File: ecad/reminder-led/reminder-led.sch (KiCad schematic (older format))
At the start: 11 parts, among them J3 MOLEX SL 1x5, Q2 2N3904, Q3 2N3904, Q4 2N3904

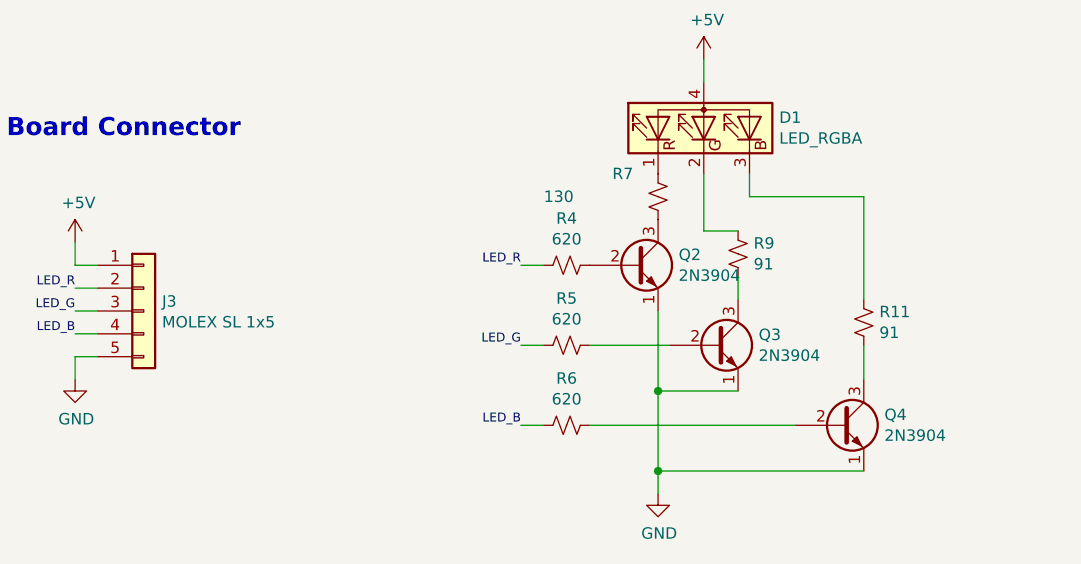
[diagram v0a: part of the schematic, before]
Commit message: Broke out file structure for separate boards
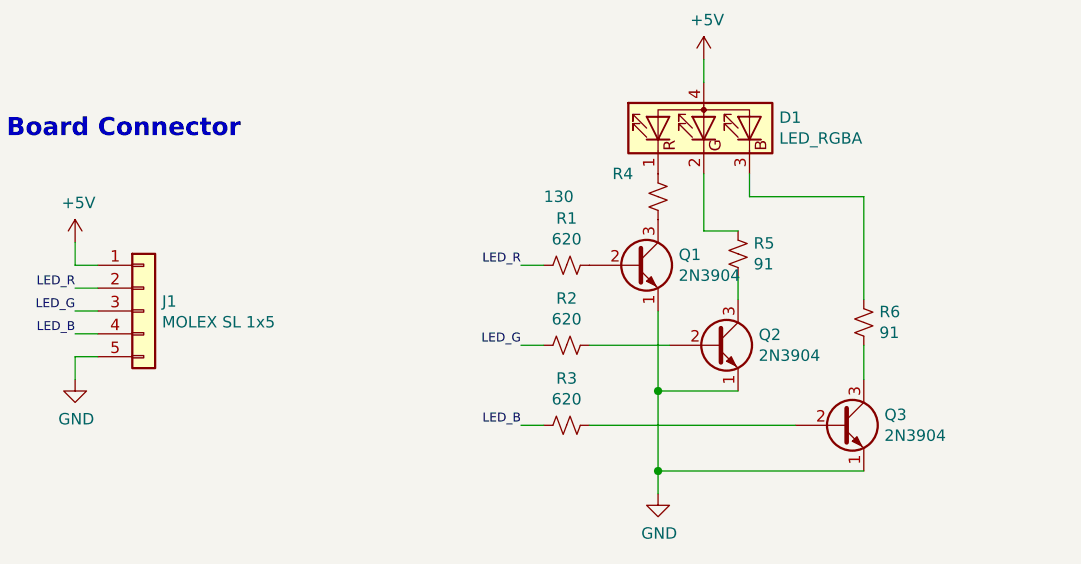
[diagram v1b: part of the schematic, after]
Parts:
- J1: renamed from J3; DNP (none) -> 1
- Q1: renamed from Q2; DNP (none) -> 1
- Q2: renamed from Q3; DNP (none) -> 1
- Q3: renamed from Q4; DNP (none) -> 1
- R1: renamed from R4; footprint Resistor_THT:R_Axial_DIN0204_L3.6mm_D1.6mm_P5.08mm_Horizontal -> R_Axial_DIN0204_L3.6mm_D1.6mm_P5.08mm_Horizontal; DNP (none) -> 1
- R2: renamed from R5; footprint Resistor_THT:R_Axial_DIN0204_L3.6mm_D1.6mm_P5.08mm_Horizontal -> R_Axial_DIN0204_L3.6mm_D1.6mm_P5.08mm_Horizontal; DNP (none) -> 1
- R3: renamed from R6; footprint Resistor_THT:R_Axial_DIN0204_L3.6mm_D1.6mm_P5.08mm_Horizontal -> R_Axial_DIN0204_L3.6mm_D1.6mm_P5.08mm_Horizontal; DNP (none) -> 1
- R4: renamed from R7; DNP (none) -> 1
- R5: renamed from R9; DNP (none) -> 1
- R6: renamed from R11; DNP (none) -> 1
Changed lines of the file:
@@
 P 6400 2650
 AR Path="/607C1B9E" Ref="#PWR?"  Part="1"
-AR Path="/60793C3B/607C1B9E" Ref="#PWR0107"  Part="1"
-F 0 "#PWR0107" H 6400 2500 50  0001 C CNN
+AR Path="/60793C3B/607C1B9E" Ref="#PWR04"  Part="1"
+F 0 "#PWR04" H 6400 2500 50  0001 C CNN
 F 1 "+5V" H 6415 2823 50  0000 C CNN
 F 2 "" H 6400 2650 50  0001 C CNN
@@
 P 5800 4250
 AR Path="/607C1BA9" Ref="R?"  Part="1"
-AR Path="/60793C3B/607C1BA9" Ref="R6"  Part="1"
-F 0 "R6" V 6005 4250 50  0000 C CNN
+AR Path="/60793C3B/607C1BA9" Ref="R3"  Part="1"
+F 0 "R3" V 6005 4250 50  0000 C CNN
 F 1 "620" V 5914 4250 50  0000 C CNN
-F 2 "Resistor_THT:R_Axial_DIN0204_L3.6mm_D1.6mm_P5.08mm_Horizontal" H 5800 4250 50  0001 C CNN
+F 2 "R_Axial_DIN0204_L3.6mm_D1.6mm_P5.08mm_Horizontal" H 5800 4250 50  0001 C CNN
 F 3 "~" H 5800 4250 50  0001 C CNN
 F 4 "Vishay" H 5800 4250 50  0001 C CNN "Mfg"
 F 5 "MBA02040C6200FC100" H 5800 4250 50  0001 C CNN "Mfg PN"
+F 6 "1" H 5800 4250 50  0001 C CNN "DNP"
 	1    5800 4250
 	0    -1   -1   0
@@
 P 5800 3900
 AR Path="/607C1BB1" Ref="R?"  Part="1"
-AR Path="/60793C3B/607C1BB1" Ref="R5"  Part="1"
-F 0 "R5" V 6005 3900 50  0000 C CNN
+AR Path="/60793C3B/607C1BB1" Ref="R2"  Part="1"
+F 0 "R2" V 6005 3900 50  0000 C CNN
 F 1 "620" V 5914 3900 50  0000 C CNN
-F 2 "Resistor_THT:R_Axial_DIN0204_L3.6mm_D1.6mm_P5.08mm_Horizontal" H 5800 3900 50  0001 C CNN
+F 2 "R_Axial_DIN0204_L3.6mm_D1.6mm_P5.08mm_Horizontal" H 5800 3900 50  0001 C CNN
 F 3 "~" H 5800 3900 50  0001 C CNN
 F 4 "Vishay" H 5800 3900 50  0001 C CNN "Mfg"
 F 5 "MBA02040C6200FC100" H 5800 3900 50  0001 C CNN "Mfg PN"
+F 6 "1" H 5800 3900 50  0001 C CNN "DNP"
 	1    5800 3900
 	0    -1   -1   0
@@
 P 5800 3550
 AR Path="/607C1BB9" Ref="R?"  Part="1"
-AR Path="/60793C3B/607C1BB9" Ref="R4"  Part="1"
-F 0 "R4" V 6005 3550 50  0000 C CNN
+AR Path="/60793C3B/607C1BB9" Ref="R1"  Part="1"
+F 0 "R1" V 6005 3550 50  0000 C CNN
 F 1 "620" V 5914 3550 50  0000 C CNN
-F 2 "Resistor_THT:R_Axial_DIN0204_L3.6mm_D1.6mm_P5.08mm_Horizontal" H 5800 3550 50  0001 C CNN
+F 2 "R_Axial_DIN0204_L3.6mm_D1.6mm_P5.08mm_Horizontal" H 5800 3550 50  0001 C CNN
 F 3 "~" H 5800 3550 50  0001 C CNN
 F 4 "Vishay" H 5800 3550 50  0001 C CNN "Mfg"
 F 5 "MBA02040C6200FC100" H 5800 3550 50  0001 C CNN "Mfg PN"
+F 6 "1" H 5800 3550 50  0001 C CNN "DNP"
 	1    5800 3550
 	0    -1   -1   0
@@
 P 6200 4550
 AR Path="/607C1BC6" Ref="#PWR?"  Part="1"
-AR Path="/60793C3B/607C1BC6" Ref="#PWR0110"  Part="1"
-F 0 "#PWR0110" H 6200 4300 50  0001 C CNN
+AR Path="/60793C3B/607C1BC6" Ref="#PWR03"  Part="1"
+F 0 "#PWR03" H 6200 4300 50  0001 C CNN
 F 1 "GND" H 6205 4377 50  0000 C CNN
 F 2 "" H 6200 4550 50  0001 C CNN
@@
 P 7100 3800
 AR Path="/607C1BD3" Ref="R?"  Part="1"
-AR Path="/60793C3B/607C1BD3" Ref="R11"  Part="1"
-F 0 "R11" H 7168 3846 50  0000 L CNN
+AR Path="/60793C3B/607C1BD3" Ref="R6"  Part="1"
+F 0 "R6" H 7168 3846 50  0000 L CNN
 F 1 "91" H 7168 3755 50  0000 L CNN
 F 2 "Resistor_THT:R_Axial_DIN0204_L3.6mm_D1.6mm_P5.08mm_Horizontal" H 7100 3800 50  0001 C CNN
 F 3 "~" H 7100 3800 50  0001 C CNN
+F 4 "1" H 7100 3800 50  0001 C CNN "DNP"
 	1    7100 3800
 	1    0    0    -1
@@
 P 6550 3500
 AR Path="/607C1BD9" Ref="R?"  Part="1"
-AR Path="/60793C3B/607C1BD9" Ref="R9"  Part="1"
-F 0 "R9" H 6618 3546 50  0000 L CNN
+AR Path="/60793C3B/607C1BD9" Ref="R5"  Part="1"
+F 0 "R5" H 6618 3546 50  0000 L CNN
 F 1 "91" H 6618 3455 50  0000 L CNN
 F 2 "Resistor_THT:R_Axial_DIN0204_L3.6mm_D1.6mm_P5.08mm_Horizontal" H 6550 3500 50  0001 C CNN
 F 3 "~" H 6550 3500 50  0001 C CNN
+F 4 "1" H 6550 3500 50  0001 C CNN "DNP"
 	1    6550 3500
 	1    0    0    -1
@@
 P 6200 3250
 AR Path="/607C1BDF" Ref="R?"  Part="1"
-AR Path="/60793C3B/607C1BDF" Ref="R7"  Part="1"
-F 0 "R7" H 6000 3350 50  0000 L CNN
+AR Path="/60793C3B/607C1BDF" Ref="R4"  Part="1"
+F 0 "R4" H 6000 3350 50  0000 L CNN
 F 1 "130" H 5700 3250 50  0000 L CNN
 F 2 "Resistor_THT:R_Axial_DIN0204_L3.6mm_D1.6mm_P5.08mm_Horizontal" H 6200 3250 50  0001 C CNN
 F 3 "~" H 6200 3250 50  0001 C CNN
+F 4 "1" H 6200 3250 50  0001 C CNN "DNP"
 	1    6200 3250
 	1    0    0    -1
@@
 P 7000 4250
 AR Path="/607C1BE5" Ref="Q?"  Part="1"
-AR Path="/60793C3B/607C1BE5" Ref="Q4"  Part="1"
-F 0 "Q4" H 7190 4296 50  0000 L CNN
+AR Path="/60793C3B/607C1BE5" Ref="Q3"  Part="1"
+F 0 "Q3" H 7190 4296 50  0000 L CNN
 F 1 "2N3904" H 7190 4205 50  0000 L CNN
 F 2 "Package_TO_SOT_THT:TO-92_Inline" H 7200 4175 50  0001 L CIN
 F 3 "https://www.fairchildsemi.com/datasheets/2N/2N3904.pdf" H 7000 4250 50  0001 L CNN
+F 4 "1" H 7000 4250 50  0001 C CNN "DNP"
 	1    7000 4250
 	1    0    0    -1
@@
 P 6450 3900
 AR Path="/607C1BEB" Ref="Q?"  Part="1"
-AR Path="/60793C3B/607C1BEB" Ref="Q3"  Part="1"
-F 0 "Q3" H 6640 3946 50  0000 L CNN
+AR Path="/60793C3B/607C1BEB" Ref="Q2"  Part="1"
+F 0 "Q2" H 6640 3946 50  0000 L CNN
 F 1 "2N3904" H 6640 3855 50  0000 L CNN
 F 2 "Package_TO_SOT_THT:TO-92_Inline" H 6650 3825 50  0001 L CIN
 F 3 "https://www.fairchildsemi.com/datasheets/2N/2N3904.pdf" H 6450 3900 50  0001 L CNN
+F 4 "1" H 6450 3900 50  0001 C CNN "DNP"
 	1    6450 3900
 	1    0    0    -1
@@
 P 6100 3550
 AR Path="/607C1BF1" Ref="Q?"  Part="1"
-AR Path="/60793C3B/607C1BF1" Ref="Q2"  Part="1"
-F 0 "Q2" H 6290 3596 50  0000 L CNN
+AR Path="/60793C3B/607C1BF1" Ref="Q1"  Part="1"
+F 0 "Q1" H 6290 3596 50  0000 L CNN
 F 1 "2N3904" H 6290 3505 50  0000 L CNN
 F 2 "Package_TO_SOT_THT:TO-92_Inline" H 6300 3475 50  0001 L CIN
 F 3 "https://www.fairchildsemi.com/datasheets/2N/2N3904.pdf" H 6100 3550 50  0001 L CNN
+F 4 "1" H 6100 3550 50  0001 C CNN "DNP"
 	1    6100 3550
 	1    0    0    -1
@@
 LED_GND
 $Comp
-L Connector_Generic:Conn_01x05 J3
+L Connector_Generic:Conn_01x05 J1
 U 1 1 607EAE28
 P 3950 3750
-F 0 "J3" H 4030 3792 50  0000 L CNN
+F 0 "J1" H 4030 3792 50  0000 L CNN
 F 1 "MOLEX SL 1x5" H 4030 3701 50  0000 L CNN
 F 2 "Connector_Molex:Molex_SL_171971-0005_1x05_P2.54mm_Vertical" H 3950 3750 50  0001 C CNN
 F 3 "~" H 3950 3750 50  0001 C CNN
+F 4 "1" H 3950 3750 50  0001 C CNN "DNP"
 	1    3950 3750
 	1    0    0    -1
@@
 P 10500 900
 AR Path="/607EFB8C" Ref="#PWR?"  Part="1"
-AR Path="/60793C3B/607EFB8C" Ref="#PWR0111"  Part="1"
-F 0 "#PWR0111" H 10500 750 50  0001 C CNN
+AR Path="/60793C3B/607EFB8C" Ref="#PWR05"  Part="1"
+F 0 "#PWR05" H 10500 750 50  0001 C CNN
 F 1 "+5V" H 10515 1073 50  0000 C CNN
 F 2 "" H 10500 900 50  0001 C CNN
@@
 P 10500 2050
 AR Path="/607F0332" Ref="#PWR?"  Part="1"
-AR Path="/60793C3B/607F0332" Ref="#PWR0129"  Part="1"
-F 0 "#PWR0129" H 10500 1800 50  0001 C CNN
+AR Path="/60793C3B/607F0332" Ref="#PWR06"  Part="1"
+F 0 "#PWR06" H 10500 1800 50  0001 C CNN
 F 1 "GND" H 10505 1877 50  0000 C CNN
 F 2 "" H 10500 2050 50  0001 C CNN
@@
 P 3650 3450
 AR Path="/60806A63" Ref="#PWR?"  Part="1"
-AR Path="/60793C3B/60806A63" Ref="#PWR0130"  Part="1"
-F 0 "#PWR0130" H 3650 3300 50  0001 C CNN
+AR Path="/60793C3B/60806A63" Ref="#PWR01"  Part="1"
+F 0 "#PWR01" H 3650 3300 50  0001 C CNN
 F 1 "+5V" H 3665 3623 50  0000 C CNN
 F 2 "" H 3650 3450 50  0001 C CNN
@@
 P 3650 4050
 AR Path="/60806E3B" Ref="#PWR?"  Part="1"
-AR Path="/60793C3B/60806E3B" Ref="#PWR0131"  Part="1"
-F 0 "#PWR0131" H 3650 3800 50  0001 C CNN
+AR Path="/60793C3B/60806E3B" Ref="#PWR02"  Part="1"
+F 0 "#PWR02" H 3650 3800 50  0001 C CNN
 F 1 "GND" H 3655 3877 50  0000 C CNN
 F 2 "" H 3650 4050 50  0001 C CNN
